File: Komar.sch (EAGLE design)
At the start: 112 parts, among them CON1 USB-VERTICAL, CON10 PINHEAD_1X01-2, CON11 PINHEAD_1X01-2, CON12 PINHEAD_1X01-2, CON13 PINHEAD_1X01-2, CON14 PINHEAD_1X01-2, CON15 PINHEAD_1X01-2, CON2 PINHEAD_1X01-2, CON3 CON-4P-TABS-STRAIGHT, CON4 CON-4P-TABS-STRAIGHT, CON5 CON-4P-TABS-STRAIGHT, CON6 CON-4P-TABS-STRAIGHT, CON7 CON-4P-TABS-STRAIGHT, CON8 PINHEAD_1X04-2, CON9 PINHEAD_1X01-2, IC1 TPD3S014DBVR-SOT23-6, IC2 TPD3S014DBVR-SOT23-6, IC3 ATA6561-GBQW-N-HVSON8, IC4 ATA6561-GBQW-N-HVSON8, IC5 MCP9700AT-E/TTVAO-SOT23, IC6 11LC040T-E/TT, Q1 FDMS86368-F085, Q10 FDMS86368-F085, Q11 FDMS86368-F085, Q12 FDMS86368-F085, Q2 FDMS86368-F085, Q3 FDMS86368-F085, Q4 FDMS86368-F085, Q5 FDMS86368-F085, Q6 FDMS86368-F085, Q7 FDMS86368-F085, Q8 FDMS86368-F085, Q9 FDMS86368-F085

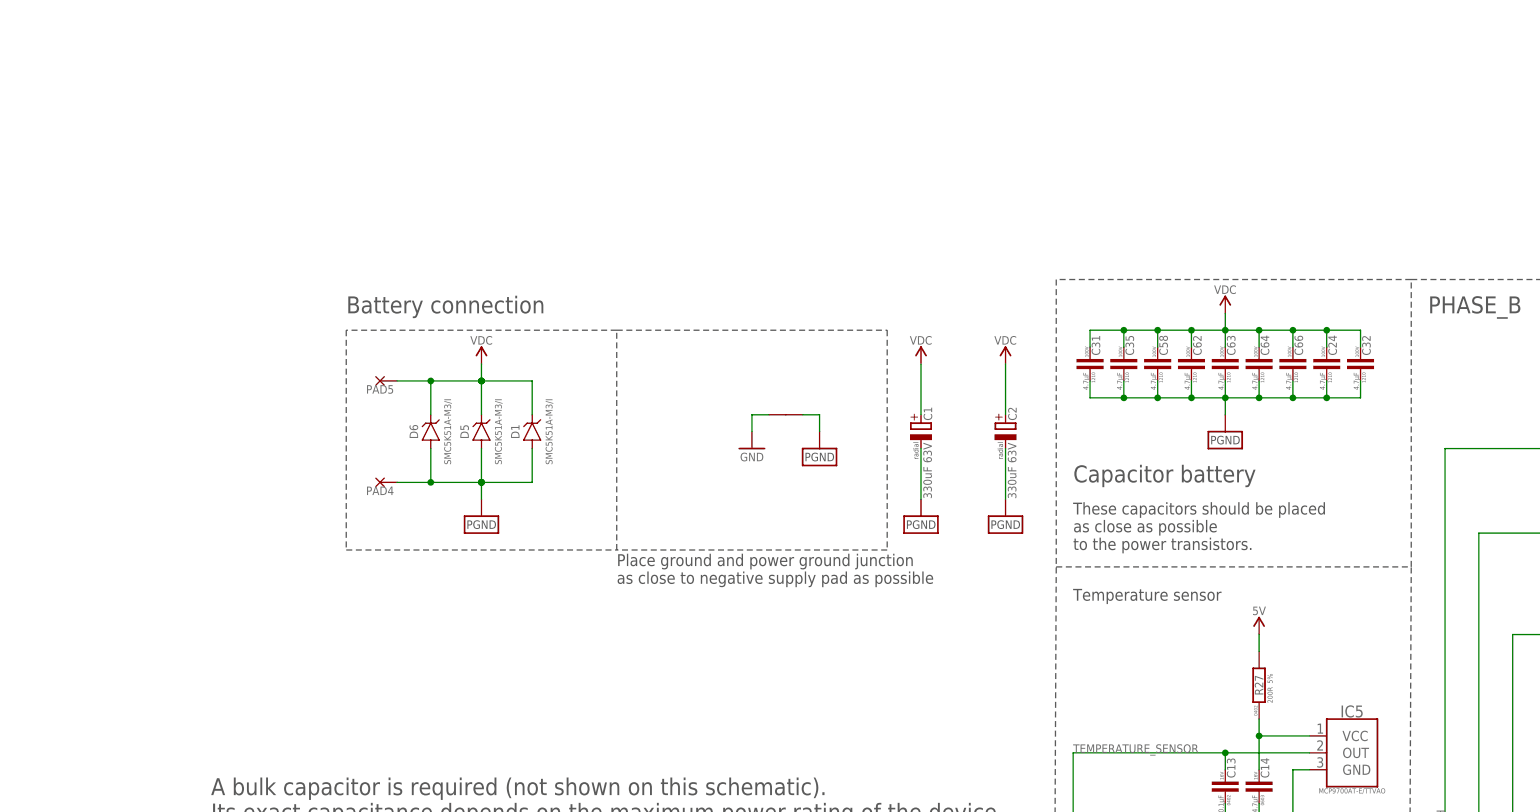
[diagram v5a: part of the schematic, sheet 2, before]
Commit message: Holes diamters for wires increased to fit AWG 14 and AWG 12 wires
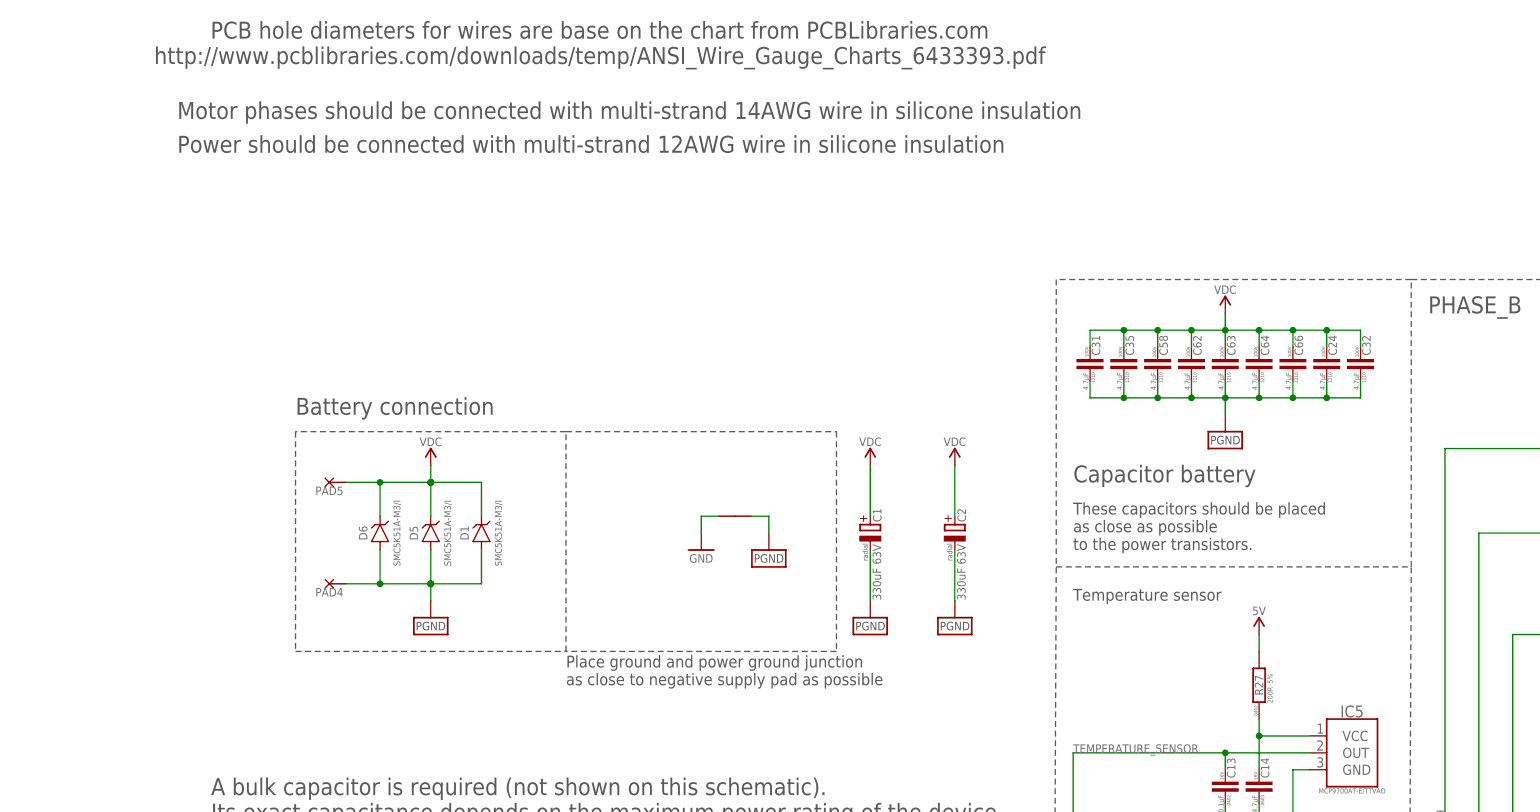
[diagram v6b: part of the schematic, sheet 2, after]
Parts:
- PAD1, PAD2, PAD3: value PAD-HOLE_2 -> PAD-HOLE_2.2_SQUARE; device PADS:PAD-HOLE_2 -> PADS:PAD-HOLE_2.2_SQUARE
- PAD4, PAD5: value PAD-HOLE_2.5 -> PAD-HOLE_2.8_SQUARE; device PADS:PAD-HOLE_2.5 -> PADS:PAD-HOLE_2.8_SQUARE
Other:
- note added: "Motor phases should be connected with multi-strand 14AWG wire in silicone insulation"
- note added: "PCB hole diameters for wires are base on the chart from PCBLibraries.com http://www.pcblibraries.com/downloads/temp/ANSI_Wire_Gauge_Charts_6433393.pdf"
- note added: "Power should be connected with multi-strand 12AWG wire in silicone insulation"
- moved on the sheet: C1, C2, D1, D5, D6, PAD4, PAD5

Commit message: Phase wires holes diameter further increased
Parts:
- PAD1, PAD2, PAD3: value PAD-HOLE_2.2_SQUARE -> PAD-HOLE_2.4_SQUARE; device PADS:PAD-HOLE_2.2_SQUARE -> PADS:PAD-HOLE_2.4_SQUARE
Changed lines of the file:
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@@
 <part name="Q2" library="mosfet" library_urn="urn:adsk.eagle:library:2640523" deviceset="FDMS86368-F085" device="" package3d_urn="urn:adsk.eagle:package:19980482/4"/>
 <part name="Q1" library="mosfet" library_urn="urn:adsk.eagle:library:2640523" deviceset="FDMS86368-F085" device="" package3d_urn="urn:adsk.eagle:package:19980482/4"/>
-<part name="PAD1" library="PADS" library_urn="urn:adsk.eagle:library:3188696" deviceset="PAD" device="-HOLE_2.2_SQUARE" package3d_urn="urn:adsk.eagle:package:20137055/1" value="PAD-HOLE_2.2_SQUARE">
+<part name="PAD1" library="PADS" library_urn="urn:adsk.eagle:library:3188696" deviceset="PAD" device="-HOLE_2.4_SQUARE" package3d_urn="urn:adsk.eagle:package:20139479/1" value="PAD-HOLE_2.4_SQUARE">
 <variant name="BASIC" populate="no"/>
 </part>
@@
 <part name="Q6" library="mosfet" library_urn="urn:adsk.eagle:library:2640523" deviceset="FDMS86368-F085" device="" package3d_urn="urn:adsk.eagle:package:19980482/4"/>
 <part name="Q5" library="mosfet" library_urn="urn:adsk.eagle:library:2640523" deviceset="FDMS86368-F085" device="" package3d_urn="urn:adsk.eagle:package:19980482/4"/>
-<part name="PAD2" library="PADS" library_urn="urn:adsk.eagle:library:3188696" deviceset="PAD" device="-HOLE_2.2_SQUARE" package3d_urn="urn:adsk.eagle:package:20137055/1" value="PAD-HOLE_2.2_SQUARE">
+<part name="PAD2" library="PADS" library_urn="urn:adsk.eagle:library:3188696" deviceset="PAD" device="-HOLE_2.4_SQUARE" package3d_urn="urn:adsk.eagle:package:20139479/1" value="PAD-HOLE_2.4_SQUARE">
 <variant name="BASIC" populate="no"/>
 </part>
@@
 <part name="Q10" library="mosfet" library_urn="urn:adsk.eagle:library:2640523" deviceset="FDMS86368-F085" device="" package3d_urn="urn:adsk.eagle:package:19980482/4"/>
 <part name="Q9" library="mosfet" library_urn="urn:adsk.eagle:library:2640523" deviceset="FDMS86368-F085" device="" package3d_urn="urn:adsk.eagle:package:19980482/4"/>
-<part name="PAD3" library="PADS" library_urn="urn:adsk.eagle:library:3188696" deviceset="PAD" device="-HOLE_2.2_SQUARE" package3d_urn="urn:adsk.eagle:package:20137055/1" value="PAD-HOLE_2.2_SQUARE">
+<part name="PAD3" library="PADS" library_urn="urn:adsk.eagle:library:3188696" deviceset="PAD" device="-HOLE_2.4_SQUARE" package3d_urn="urn:adsk.eagle:package:20139479/1" value="PAD-HOLE_2.4_SQUARE">
 <variant name="BASIC" populate="no"/>
 </part>
@@
 <attribute name="VOLTAGE" value="100V"/>
 </part>
-<part name="PAD4" library="PADS" library_urn="urn:adsk.eagle:library:3188696" deviceset="PAD" device="-HOLE_2.8_SQUARE" value="PAD-HOLE_2.8_SQUARE">
+<part name="PAD4" library="PADS" library_urn="urn:adsk.eagle:library:3188696" deviceset="PAD" device="-HOLE_2.8_SQUARE" package3d_urn="urn:adsk.eagle:package:20139477/1" value="PAD-HOLE_2.8_SQUARE">
 <variant name="BASIC" populate="no"/>
 </part>
-<part name="PAD5" library="PADS" library_urn="urn:adsk.eagle:library:3188696" deviceset="PAD" device="-HOLE_2.8_SQUARE" value="PAD-HOLE_2.8_SQUARE">
+<part name="PAD5" library="PADS" library_urn="urn:adsk.eagle:library:3188696" deviceset="PAD" device="-HOLE_2.8_SQUARE" package3d_urn="urn:adsk.eagle:package:20139477/1" value="PAD-HOLE_2.8_SQUARE">
 <variant name="BASIC" populate="no"/>
 </part>
@@
 <segment>
 <pinref part="IC5" gate="G$1" pin="OUT"/>
-<wire x1="175.26" y1="180.34" x2="162.56" y2="180.34" width="0.1524" layer="91"/>
-<wire x1="162.56" y1="177.8" x2="162.56" y2="180.34" width="0.1524" layer="91"/>
-<junction x="162.56" y="180.34"/>
+<wire x1="175.26" y1="180.34" x2="165.1" y2="182.88" width="0.1524" layer="91"/>
+<wire x1="162.56" y1="177.8" x2="165.1" y2="182.88" width="0.1524" layer="91"/>
+<junction x="165.1" y="182.88"/>
 <pinref part="C13" gate="G$1" pin="2"/>
-<wire x1="139.7" y1="180.34" x2="162.56" y2="180.34" width="0.1524" layer="91"/>
-<wire x1="139.7" y1="149.86" x2="139.7" y2="180.34" width="0.1524" layer="91"/>
+<wire x1="142.24" y1="182.88" x2="165.1" y2="182.88" width="0.1524" layer="91"/>
+<wire x1="139.7" y1="149.86" x2="142.24" y2="182.88" width="0.1524" layer="91"/>
 <label x="139.7" y="180.34" size="1.27" layer="95" font="vector"/>
 </segment>

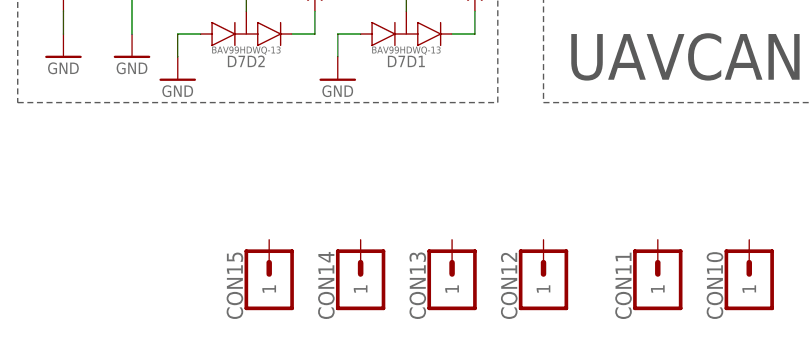
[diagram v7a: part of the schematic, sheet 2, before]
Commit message: minor silkscreen updates
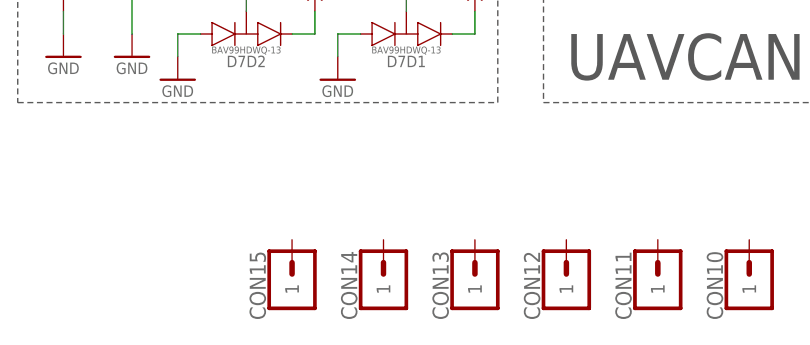
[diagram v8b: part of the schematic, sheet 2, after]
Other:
- moved on the sheet: CON12, CON13, CON14, CON15
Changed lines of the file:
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@@
 </part>
 <part name="+P16" library="supply_symbols" library_urn="urn:adsk.eagle:library:5017758" deviceset="5V" device=""/>
-<part name="CON2" library="pinhead" library_urn="urn:adsk.eagle:library:2540341" deviceset="PINHEAD_1X01" device="-2" package3d_urn="urn:adsk.eagle:package:2540397/3">
+<part name="CON2" library="pinhead" library_urn="urn:adsk.eagle:library:2540341" deviceset="PINHEAD_1X01" device="-2" package3d_urn="urn:adsk.eagle:package:2540397/4">
 <variant name="BASIC" populate="no"/>
 </part>
-<part name="CON9" library="pinhead" library_urn="urn:adsk.eagle:library:2540341" deviceset="PINHEAD_1X01" device="-2" package3d_urn="urn:adsk.eagle:package:2540397/3">
+<part name="CON9" library="pinhead" library_urn="urn:adsk.eagle:library:2540341" deviceset="PINHEAD_1X01" device="-2" package3d_urn="urn:adsk.eagle:package:2540397/4">
 <variant name="BASIC" populate="no"/>
 </part>
@@
 <part name="+P25" library="supply_symbols" library_urn="urn:adsk.eagle:library:5017758" deviceset="5V" device=""/>
 <part name="GND47" library="supply_symbols" library_urn="urn:adsk.eagle:library:5017758" deviceset="GND" device="" value="GND"/>
-<part name="CON8" library="pinhead" library_urn="urn:adsk.eagle:library:2540341" deviceset="PINHEAD_1X04" device="-2" package3d_urn="urn:adsk.eagle:package:4854340/3">
+<part name="CON8" library="pinhead" library_urn="urn:adsk.eagle:library:2540341" deviceset="PINHEAD_1X04" device="-2" package3d_urn="urn:adsk.eagle:package:4854340/4">
 <variant name="BASIC" populate="no"/>
 </part>
-<part name="CON10" library="pinhead" library_urn="urn:adsk.eagle:library:2540341" deviceset="PINHEAD_1X01" device="-2" package3d_urn="urn:adsk.eagle:package:2540397/3"/>
-<part name="CON11" library="pinhead" library_urn="urn:adsk.eagle:library:2540341" deviceset="PINHEAD_1X01" device="-2" package3d_urn="urn:adsk.eagle:package:2540397/3"/>
-<part name="CON12" library="pinhead" library_urn="urn:adsk.eagle:library:2540341" deviceset="PINHEAD_1X01" device="-2" package3d_urn="urn:adsk.eagle:package:2540397/3"/>
-<part name="CON13" library="pinhead" library_urn="urn:adsk.eagle:library:2540341" deviceset="PINHEAD_1X01" device="-2" package3d_urn="urn:adsk.eagle:package:2540397/3"/>
-<part name="CON14" library="pinhead" library_urn="urn:adsk.eagle:library:2540341" deviceset="PINHEAD_1X01" device="-2" package3d_urn="urn:adsk.eagle:package:2540397/3"/>
-<part name="CON15" library="pinhead" library_urn="urn:adsk.eagle:library:2540341" deviceset="PINHEAD_1X01" device="-2" package3d_urn="urn:adsk.eagle:package:2540397/3"/>
+<part name="CON10" library="pinhead" library_urn="urn:adsk.eagle:library:2540341" deviceset="PINHEAD_1X01" device="-2" package3d_urn="urn:adsk.eagle:package:2540397/4">
+<variant name="BASIC" populate="no"/>
+</part>
+<part name="CON11" library="pinhead" library_urn="urn:adsk.eagle:library:2540341" deviceset="PINHEAD_1X01" device="-2" package3d_urn="urn:adsk.eagle:package:2540397/4">
+<variant name="BASIC" populate="no"/>
+</part>
+<part name="CON12" library="pinhead" library_urn="urn:adsk.eagle:library:2540341" deviceset="PINHEAD_1X01" device="-2" package3d_urn="urn:adsk.eagle:package:2540397/4">
+<variant name="BASIC" populate="no"/>
+</part>
+<part name="CON13" library="pinhead" library_urn="urn:adsk.eagle:library:2540341" deviceset="PINHEAD_1X01" device="-2" package3d_urn="urn:adsk.eagle:package:2540397/4">
+<variant name="BASIC" populate="no"/>
+</part>
+<part name="CON14" library="pinhead" library_urn="urn:adsk.eagle:library:2540341" deviceset="PINHEAD_1X01" device="-2" package3d_urn="urn:adsk.eagle:package:2540397/4">
+<variant name="BASIC" populate="no"/>
+</part>
+<part name="CON15" library="pinhead" library_urn="urn:adsk.eagle:library:2540341" deviceset="PINHEAD_1X01" device="-2" package3d_urn="urn:adsk.eagle:package:2540397/4">
+<variant name="BASIC" populate="no"/>
+</part>
 </parts>
 <sheets>
@@
 <attribute name="NAME" x="247.65" y="10.16" size="1.778" layer="95" font="vector" ratio="15" rot="R90" align="center"/>
 </instance>
-<instance part="CON12" gate="G$1" x="241.3" y="7.62" smashed="yes" rot="R90">
-<attribute name="NAME" x="234.95" y="10.16" size="1.778" layer="95" font="vector" ratio="15" rot="R90" align="center"/>
-</instance>
-<instance part="CON13" gate="G$1" x="231.14" y="7.62" smashed="yes" rot="R90">
-<attribute name="NAME" x="224.79" y="10.16" size="1.778" layer="95" font="vector" ratio="15" rot="R90" align="center"/>
-</instance>
-<instance part="CON14" gate="G$1" x="220.98" y="7.62" smashed="yes" rot="R90">
-<attribute name="NAME" x="214.63" y="10.16" size="1.778" layer="95" font="vector" ratio="15" rot="R90" align="center"/>
-</instance>
-<instance part="CON15" gate="G$1" x="210.82" y="7.62" smashed="yes" rot="R90">
-<attribute name="NAME" x="204.47" y="10.16" size="1.778" layer="95" font="vector" ratio="15" rot="R90" align="center"/>
+<instance part="CON12" gate="G$1" x="243.84" y="7.62" smashed="yes" rot="R90">
+<attribute name="NAME" x="237.49" y="10.16" size="1.778" layer="95" font="vector" ratio="15" rot="R90" align="center"/>
+</instance>
+<instance part="CON13" gate="G$1" x="233.68" y="7.62" smashed="yes" rot="R90">
+<attribute name="NAME" x="227.33" y="10.16" size="1.778" layer="95" font="vector" ratio="15" rot="R90" align="center"/>
+</instance>
+<instance part="CON14" gate="G$1" x="223.52" y="7.62" smashed="yes" rot="R90">
+<attribute name="NAME" x="217.17" y="10.16" size="1.778" layer="95" font="vector" ratio="15" rot="R90" align="center"/>
+</instance>
+<instance part="CON15" gate="G$1" x="213.36" y="7.62" smashed="yes" rot="R90">
+<attribute name="NAME" x="207.01" y="10.16" size="1.778" layer="95" font="vector" ratio="15" rot="R90" align="center"/>
 </instance>
 </instances>
